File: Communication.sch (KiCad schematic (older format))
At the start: 24 parts, among them IC1 LAN8720

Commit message: added some footprints
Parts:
- renumbered C41 to C201, C18 to C202, C19 to C203, C20 to C204, C21 to C205, C22 to C206, C23 to C207, C24 to C208, C25 to C209, C26 to C210, C38 to C211, IC1 to IC201, L1 to L201, R7 to R201, R12 to R202, R13 to R203, R14 to R204, R15 to R205, R16 to R206, R17 to R207, R18 to R208, R19 to R209, R20 to R210, R21 to R211
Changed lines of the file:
@@
 $EndDescr
 $Comp
-L LAN8720 IC1
+L LAN8720 IC201
 U 1 1 560279E6
 P 3150 6150
-F 0 "IC1" H 2650 7650 60  0000 C CNN
+F 0 "IC201" H 2650 7650 60  0000 C CNN
 F 1 "LAN8720" H 3600 7650 60  0000 C CNN
 F 2 "Communication:LAN8720_QFN33" H 2250 -2125 60  0001 C CNN
@@
 ~RESET
 $Comp
-L R R16
+L R R206
 U 1 1 5631F773
 P 2250 4600
-F 0 "R16" V 2330 4600 50  0000 C CNN
+F 0 "R206" V 2330 4600 50  0000 C CNN
 F 1 "10k" V 2175 4600 50  0000 C CNN
 F 2 "Passives:R0402N" V 2180 4600 30  0001 C CNN
@@
 $EndComp
 $Comp
-L R R15
+L R R205
 U 1 1 5631F817
 P 2000 4600
-F 0 "R15" V 2080 4600 50  0000 C CNN
+F 0 "R205" V 2080 4600 50  0000 C CNN
 F 1 "1k" V 1925 4600 50  0000 C CNN
 F 2 "Passives:R0402N" V 1930 4600 30  0001 C CNN
@@
 $EndComp
 $Comp
-L R R7
+L R R201
 U 1 1 5631FB19
 P 1750 4600
-F 0 "R7" V 1830 4600 50  0000 C CNN
+F 0 "R201" V 1830 4600 50  0000 C CNN
 F 1 "10k" V 1675 4600 50  0000 C CNN
 F 2 "Passives:R0402N" V 1680 4600 30  0001 C CNN
@@
 $EndComp
 $Comp
-L R R13
+L R R203
 U 1 1 5631FC48
 P 1800 7150
-F 0 "R13" V 1880 7150 50  0000 C CNN
+F 0 "R203" V 1880 7150 50  0000 C CNN
 F 1 "10k" V 1725 7150 50  0000 C CNN
 F 2 "Passives:R0402N" V 1730 7150 30  0001 C CNN
@@
 $EndComp
 $Comp
-L R R17
+L R R207
 U 1 1 5632002D
 P 4050 6500
-F 0 "R17" V 4130 6500 50  0000 C CNN
+F 0 "R207" V 4130 6500 50  0000 C CNN
 F 1 "12k" V 3975 6500 50  0000 C CNN
 F 2 "Passives:R0402N" V 3980 6500 30  0001 C CNN
@@
 $EndComp
 $Comp
-L R R14
+L R R204
 U 1 1 56320375
 P 1800 7450
-F 0 "R14" V 1880 7450 50  0000 C CNN
+F 0 "R204" V 1880 7450 50  0000 C CNN
 F 1 "470" V 1725 7450 50  0000 C CNN
 F 2 "Passives:R0402N" V 1730 7450 30  0001 C CNN
@@
 $EndComp
 $Comp
-L GND #PWR0140
+L GND #PWR074
 U 1 1 56320982
 P 1600 7150
-F 0 "#PWR0140" H 1600 6900 50  0001 C CNN
+F 0 "#PWR074" H 1600 6900 50  0001 C CNN
 F 1 "GND" H 1600 7000 50  0000 C CNN
 F 2 "" H 1600 7150 60  0000 C CNN
@@
 ETH_LED_ACT+
 $Comp
-L +3V3 #PWR0141
+L +3V3 #PWR075
 U 1 1 5632140A
 P 1750 4400
-F 0 "#PWR0141" H 1750 4250 50  0001 C CNN
+F 0 "#PWR075" H 1750 4250 50  0001 C CNN
 F 1 "+3V3" H 1750 4540 50  0000 C CNN
 F 2 "" H 1750 4400 60  0000 C CNN
@@
 $EndComp
 $Comp
-L +3V3 #PWR0142
+L +3V3 #PWR076
 U 1 1 5632147E
 P 2000 4400
-F 0 "#PWR0142" H 2000 4250 50  0001 C CNN
+F 0 "#PWR076" H 2000 4250 50  0001 C CNN
 F 1 "+3V3" H 2000 4540 50  0000 C CNN
 F 2 "" H 2000 4400 60  0000 C CNN
@@
 $EndComp
 $Comp
-L +3V3 #PWR0143
+L +3V3 #PWR077
 U 1 1 563214F2
 P 2250 4400
-F 0 "#PWR0143" H 2250 4250 50  0001 C CNN
+F 0 "#PWR077" H 2250 4250 50  0001 C CNN
 F 1 "+3V3" H 2250 4540 50  0000 C CNN
 F 2 "" H 2250 4400 60  0000 C CNN
@@
 $EndComp
 $Comp
-L C C19
+L C C203
 U 1 1 56322113
 P 4400 6500
-F 0 "C19" H 4450 6600 50  0000 L CNN
-F 1 "1u,10V,X5R" H 4450 6400 50  0000 L CNN
+F 0 "C203" H 4450 6600 50  0000 L CNN
+F 1 "1u,10V,X5R" V 4550 6150 50  0000 L CNN
 F 2 "Passives:C0402N" H 4438 6350 30  0001 C CNN
 F 3 "" H 4450 6600 60  0000 C CNN
@@
 $EndComp
 $Comp
-L C C20
+L C C204
 U 1 1 56322340
 P 4650 6500
-F 0 "C20" H 4700 6600 50  0000 L CNN
-F 1 "1u,10V,X5R" H 4700 6400 50  0000 L CNN
+F 0 "C204" H 4700 6600 50  0000 L CNN
+F 1 "1u,10V,X5R" V 4750 6100 50  0000 L CNN
 F 2 "Passives:C0402N" H 4688 6350 30  0001 C CNN
 F 3 "" H 4700 6600 60  0000 C CNN
@@
 $EndComp
 $Comp
-L C C21
+L C C205
 U 1 1 563223C9
 P 4900 6500
-F 0 "C21" H 4950 6600 50  0000 L CNN
-F 1 "1u,10V,X5R" H 4950 6400 50  0000 L CNN
+F 0 "C205" H 4950 6600 50  0000 L CNN
+F 1 "1u,10V,X5R" V 5000 6100 50  0000 L CNN
 F 2 "Passives:C0402N" H 4938 6350 30  0001 C CNN
 F 3 "" H 4950 6600 60  0000 C CNN
@@
 $EndComp
 $Comp
-L C C22
+L C C206
 U 1 1 56322451
 P 5150 6500
-F 0 "C22" H 5200 6600 50  0000 L CNN
-F 1 "1u,10V,X5R" H 5200 6400 50  0000 L CNN
+F 0 "C206" H 5200 6600 50  0000 L CNN
+F 1 "1u,10V,X5R" V 5250 6100 50  0000 L CNN
 F 2 "Passives:C0402N" H 5188 6350 30  0001 C CNN
 F 3 "" H 5200 6600 60  0000 C CNN
@@
 $EndComp
 $Comp
-L B L1
+L B L201
 U 1 1 5632291C
 P 4650 5700
-F 0 "L1" V 4730 5700 50  0000 C CNN
+F 0 "L201" V 4730 5700 50  0000 C CNN
 F 1 "600R@100M" V 4575 5700 50  0000 C CNN
 F 2 "Passives:B0402N" V 4580 5700 30  0001 C CNN
@@
 $EndComp
 $Comp
-L +3V3 #PWR0144
+L +3V3 #PWR078
 U 1 1 56322C4E
 P 5200 5450
-F 0 "#PWR0144" H 5200 5300 50  0001 C CNN
+F 0 "#PWR078" H 5200 5300 50  0001 C CNN
 F 1 "+3V3" H 5200 5590 50  0000 C CNN
 F 2 "" H 5200 5450 60  0000 C CNN
@@
 49.9R close to phy\n10p close to jack
 $Comp
-L C C23
+L C C207
 U 1 1 563232AF
 P 5400 6500
-F 0 "C23" H 5450 6600 50  0000 L CNN
+F 0 "C207" H 5450 6600 50  0000 L CNN
 F 1 "10p" H 5450 6400 50  0000 L CNN
 F 2 "Passives:C0402N" H 5438 6350 30  0001 C CNN
@@
 $EndComp
 $Comp
-L C C24
+L C C208
 U 1 1 56323419
 P 5650 6500
-F 0 "C24" H 5700 6600 50  0000 L CNN
+F 0 "C208" H 5700 6600 50  0000 L CNN
 F 1 "10p" H 5700 6400 50  0000 L CNN
 F 2 "Passives:C0402N" H 5688 6350 30  0001 C CNN
@@
 $EndComp
 $Comp
-L C C25
+L C C209
 U 1 1 563234AD
 P 5900 6500
-F 0 "C25" H 5950 6600 50  0000 L CNN
+F 0 "C209" H 5950 6600 50  0000 L CNN
 F 1 "10p" H 5950 6400 50  0000 L CNN
 F 2 "Passives:C0402N" H 5938 6350 30  0001 C CNN
@@
 $EndComp
 $Comp
-L C C26
+L C C210
 U 1 1 56323544
 P 6150 6500
-F 0 "C26" H 6200 6600 50  0000 L CNN
+F 0 "C210" H 6200 6600 50  0000 L CNN
 F 1 "10p" H 6200 6400 50  0000 L CNN
 F 2 "Passives:C0402N" H 6188 6350 30  0001 C CNN
@@
 $EndComp
 $Comp
-L R R18
+L R R208
 U 1 1 5632500E
 P 4300 4600
-F 0 "R18" V 4380 4600 50  0000 C CNN
+F 0 "R208" V 4380 4600 50  0000 C CNN
 F 1 "49.9R" V 4225 4600 50  0000 C CNN
 F 2 "Passives:R0402N" V 4230 4600 30  0001 C CNN
@@
 $EndComp
 $Comp
-L R R19
+L R R209
 U 1 1 563251C5
 P 4550 4600
-F 0 "R19" V 4630 4600 50  0000 C CNN
+F 0 "R209" V 4630 4600 50  0000 C CNN
 F 1 "49.9R" V 4475 4600 50  0000 C CNN
 F 2 "Passives:R0402N" V 4480 4600 30  0001 C CNN
@@
 $EndComp
 $Comp
-L R R20
+L R R210
 U 1 1 56325265
 P 4800 4600
-F 0 "R20" V 4880 4600 50  0000 C CNN
+F 0 "R210" V 4880 4600 50  0000 C CNN
 F 1 "49.9R" V 4725 4600 50  0000 C CNN
 F 2 "Passives:R0402N" V 4730 4600 30  0001 C CNN
@@
 $EndComp
 $Comp
-L R R21
+L R R211
 U 1 1 56325308
 P 5050 4600
-F 0 "R21" V 5130 4600 50  0000 C CNN
+F 0 "R211" V 5130 4600 50  0000 C CNN
 F 1 "49.9R" V 4975 4600 50  0000 C CNN
 F 2 "Passives:R0402N" V 4980 4600 30  0001 C CNN
@@
 $EndComp
 $Comp
-L +3V3 #PWR0145
+L +3V3 #PWR079
 U 1 1 5632575A
 P 4300 4300
-F 0 "#PWR0145" H 4300 4150 50  0001 C CNN
+F 0 "#PWR079" H 4300 4150 50  0001 C CNN
 F 1 "+3V3" H 4300 4440 50  0000 C CNN
 F 2 "" H 4300 4300 60  0000 C CNN
@@
 $EndComp
 $Comp
-L GND #PWR0146
+L GND #PWR080
 U 1 1 5632693C
 P 6600 6750
-F 0 "#PWR0146" H 6600 6500 50  0001 C CNN
+F 0 "#PWR080" H 6600 6500 50  0001 C CNN
 F 1 "GND" H 6600 6600 50  0000 C CNN
 F 2 "" H 6600 6750 60  0000 C CNN
@@
 $EndComp
 $Comp
-L C C18
+L C C202
 U 1 1 56328E06
 P 3900 4350
-F 0 "C18" H 3950 4450 50  0000 L CNN
-F 1 "1u,10V,X5R" H 3950 4250 50  0000 L CNN
+F 0 "C202" H 3950 4450 50  0000 L CNN
+F 1 "1u,10V,X5R" V 4050 4000 50  0000 L CNN
 F 2 "Passives:C0402N" H 3938 4200 30  0001 C CNN
 F 3 "" H 3950 4450 60  0000 C CNN
@@
 $EndComp
 $Comp
-L GND #PWR0147
+L GND #PWR081
 U 1 1 56328F2F
 P 3700 4350
-F 0 "#PWR0147" H 3700 4100 50  0001 C CNN
+F 0 "#PWR081" H 3700 4100 50  0001 C CNN
 F 1 "GND" H 3700 4200 50  0000 C CNN
 F 2 "" H 3700 4350 60  0000 C CNN
@@
 $EndComp
 $Comp
-L C C38
+L C C211
 U 1 1 563CF2AE
 P 6400 6500
-F 0 "C38" H 6450 6600 50  0000 L CNN
+F 0 "C211" H 6450 6600 50  0000 L CNN
 F 1 "22u,10V" H 6450 6400 50  0000 L CNN
 F 2 "Passives:C1206N" H 6438 6350 30  0001 C CNN
@@
 $EndComp
 $Comp
-L +3V3 #PWR0152
+L +3V3 #PWR082
 U 1 1 563CF909
 P 6400 6300
-F 0 "#PWR0152" H 6400 6150 50  0001 C CNN
+F 0 "#PWR082" H 6400 6150 50  0001 C CNN
 F 1 "+3V3" H 6400 6440 50  0000 C CNN
 F 2 "" H 6400 6300 60  0000 C CNN
@@
 $EndComp
 $Comp
-L C C41
+L C C201
 U 1 1 563DCD97
 P 3900 4100
-F 0 "C41" H 3950 4200 50  0000 L CNN
-F 1 "1u,10V,X5R" H 3950 4000 50  0000 L CNN
+F 0 "C201" H 3950 4200 50  0000 L CNN
+F 1 "1u,10V,X5R" V 4050 3750 50  0000 L CNN
 F 2 "Passives:C0402N" H 3938 3950 30  0001 C CNN
 F 3 "" H 3950 4200 60  0000 C CNN
@@
 $EndComp
 $Comp
-L GND #PWR0153
+L GND #PWR083
 U 1 1 563DD118
 P 3700 4100
-F 0 "#PWR0153" H 3700 3850 50  0001 C CNN
+F 0 "#PWR083" H 3700 3850 50  0001 C CNN
 F 1 "GND" H 3700 3950 50  0000 C CNN
 F 2 "" H 3700 4100 60  0000 C CNN
@@
 Connection ~ 4150 4350
 $Comp
-L R R12
+L R R202
 U 1 1 56320243
 P 1800 6800
-F 0 "R12" V 1880 6800 50  0000 C CNN
+F 0 "R202" V 1880 6800 50  0000 C CNN
 F 1 "470" V 1725 6800 50  0000 C CNN
 F 2 "Passives:R0402N" V 1730 6800 30  0001 C CNN

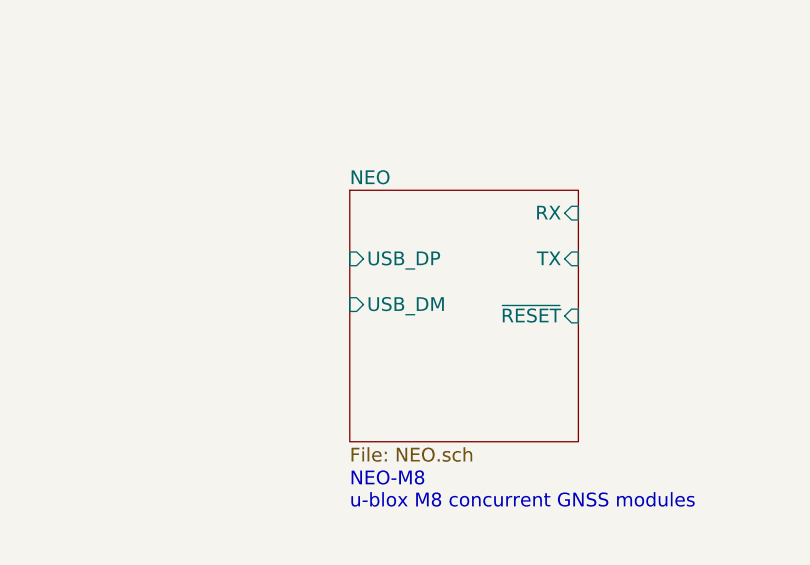
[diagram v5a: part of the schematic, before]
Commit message: adjusted 3d models
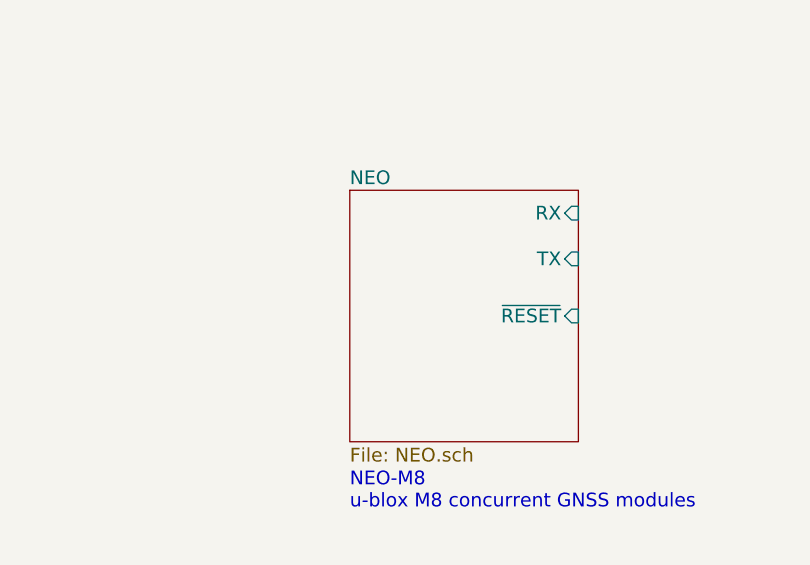
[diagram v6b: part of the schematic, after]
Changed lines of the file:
@@
 $EndComp
 $Comp
-L GND #PWR201
+L GND #PWR074
 U 1 1 56320982
 P 1600 7150
-F 0 "#PWR201" H 1600 6900 50  0001 C CNN
+F 0 "#PWR074" H 1600 6900 50  0001 C CNN
 F 1 "GND" H 1600 7000 50  0000 C CNN
 F 2 "" H 1600 7150 60  0000 C CNN
@@
 ETH_LED_ACT+
 $Comp
-L +3V3 #PWR202
+L +3V3 #PWR075
 U 1 1 5632140A
 P 1750 4400
-F 0 "#PWR202" H 1750 4250 50  0001 C CNN
+F 0 "#PWR075" H 1750 4250 50  0001 C CNN
 F 1 "+3V3" H 1750 4540 50  0000 C CNN
 F 2 "" H 1750 4400 60  0000 C CNN
@@
 $EndComp
 $Comp
-L +3V3 #PWR203
+L +3V3 #PWR076
 U 1 1 5632147E
 P 2000 4400
-F 0 "#PWR203" H 2000 4250 50  0001 C CNN
+F 0 "#PWR076" H 2000 4250 50  0001 C CNN
 F 1 "+3V3" H 2000 4540 50  0000 C CNN
 F 2 "" H 2000 4400 60  0000 C CNN
@@
 $EndComp
 $Comp
-L +3V3 #PWR204
+L +3V3 #PWR077
 U 1 1 563214F2
 P 2250 4400
-F 0 "#PWR204" H 2250 4250 50  0001 C CNN
+F 0 "#PWR077" H 2250 4250 50  0001 C CNN
 F 1 "+3V3" H 2250 4540 50  0000 C CNN
 F 2 "" H 2250 4400 60  0000 C CNN
@@
 $EndComp
 $Comp
-L +3V3 #PWR208
+L +3V3 #PWR078
 U 1 1 56322C4E
 P 5200 5450
-F 0 "#PWR208" H 5200 5300 50  0001 C CNN
+F 0 "#PWR078" H 5200 5300 50  0001 C CNN
 F 1 "+3V3" H 5200 5590 50  0000 C CNN
 F 2 "" H 5200 5450 60  0000 C CNN
@@
 $EndComp
 $Comp
-L +3V3 #PWR207
+L +3V3 #PWR079
 U 1 1 5632575A
 P 4300 4300
-F 0 "#PWR207" H 4300 4150 50  0001 C CNN
+F 0 "#PWR079" H 4300 4150 50  0001 C CNN
 F 1 "+3V3" H 4300 4440 50  0000 C CNN
 F 2 "" H 4300 4300 60  0000 C CNN
@@
 $EndComp
 $Comp
-L GND #PWR210
+L GND #PWR080
 U 1 1 5632693C
 P 6600 6750
-F 0 "#PWR210" H 6600 6500 50  0001 C CNN
+F 0 "#PWR080" H 6600 6500 50  0001 C CNN
 F 1 "GND" H 6600 6600 50  0000 C CNN
 F 2 "" H 6600 6750 60  0000 C CNN
@@
 $EndComp
 $Comp
-L GND #PWR206
+L GND #PWR081
 U 1 1 56328F2F
 P 3700 4350
-F 0 "#PWR206" H 3700 4100 50  0001 C CNN
+F 0 "#PWR081" H 3700 4100 50  0001 C CNN
 F 1 "GND" H 3700 4200 50  0000 C CNN
 F 2 "" H 3700 4350 60  0000 C CNN
@@
 $EndComp
 $Comp
-L +3V3 #PWR209
+L +3V3 #PWR082
 U 1 1 563CF909
 P 6400 6300
-F 0 "#PWR209" H 6400 6150 50  0001 C CNN
+F 0 "#PWR082" H 6400 6150 50  0001 C CNN
 F 1 "+3V3" H 6400 6440 50  0000 C CNN
 F 2 "" H 6400 6300 60  0000 C CNN
@@
 $EndComp
 $Comp
-L GND #PWR205
+L GND #PWR083
 U 1 1 563DD118
 P 3700 4100
-F 0 "#PWR205" H 3700 3850 50  0001 C CNN
+F 0 "#PWR083" H 3700 3850 50  0001 C CNN
 F 1 "GND" H 3700 3950 50  0000 C CNN
 F 2 "" H 3700 4100 60  0000 C CNN
@@
 F0 "NEO" 60
 F1 "NEO.sch" 60
-F2 "USB_DP" I L 7200 1750 60
-F3 "USB_DM" I L 7200 1950 60
-F4 "RX" I R 8200 1550 60
-F5 "TX" I R 8200 1750 60
-F6 "~RESET" I R 8200 2000 60
+F2 "RX" I R 8200 1550 60
+F3 "TX" I R 8200 1750 60
+F4 "~RESET" I R 8200 2000 60
 $EndSheet
 $EndSCHEMATC

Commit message: sorted components
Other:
- note added: "TOBY PWR_ON\nNachschlagen\n"
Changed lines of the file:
@@
 F0 "TOBY" 60
 F1 "TOBY.sch" 60
-F2 "RxD" I R 3350 1150 60
-F3 "TxD" I R 3350 1350 60
-F4 "USB_D+" I R 3350 1550 60
-F5 "USB_D-" I R 3350 1700 60
-F6 "~RESET" I L 2300 1300 60
-F7 "PWR_ON" I L 2300 1500 60
+F2 "USB_D+" I R 3350 1550 60
+F3 "USB_D-" I R 3350 1700 60
+F4 "~RESET" I L 2300 1300 60
+F5 "PWR_ON" I L 2300 1500 60
 $EndSheet
 Text Notes 2250 900  0    60   ~ 0
@@
 F4 "~RESET" I R 8200 2000 60
 $EndSheet
+Text HLabel 5950 1500 2    60   Input ~ 0
+~RESET
+Text HLabel 8400 2000 2    60   Input ~ 0
+~RESET
+Wire Wire Line
+	5650 1500 5950 1500
+Wire Wire Line
+	8200 2000 8400 2000
+Text Notes 1600 1600 0    60   ~ 0
+TOBY PWR_ON\nNachschlagen\n
+Text HLabel 5950 1000 2    60   Input ~ 0
+USB_VBUS_EN
+Text HLabel 5950 1150 2    60   Input ~ 0
+USB_VBUS_OC
+Text HLabel 5950 1300 2    60   Input ~ 0
+USB_VBUS_OUT
+Wire Wire Line
+	5650 1000 5950 1000
+Wire Wire Line
+	5650 1150 5950 1150
+Wire Wire Line
+	5650 1300 5950 1300
+Text HLabel 8550 1550 2    60   Input ~ 0
+RX_NEO
+Text HLabel 8550 1750 2    60   Input ~ 0
+TX_NEO
+Wire Wire Line
+	8200 1550 8550 1550
+Wire Wire Line
+	8200 1750 8550 1750
 $EndSCHEMATC
